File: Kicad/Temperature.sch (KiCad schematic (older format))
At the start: 2 parts

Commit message: Ready for Rev3 First layout review
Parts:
- removed TP11: CONN_1, symbol CONN_1
- R15: value 10K -> 1K
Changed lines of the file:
@@
 Sheet 4 7
 Title ""
-Date "11 oct 2014"
+Date "18 oct 2014"
 Rev ""
 Comp ""
@@
 P 3700 3300
 F 0 "R15" V 3780 3300 40  0000 C CNN
-F 1 "10K" V 3707 3301 40  0000 C CNN
+F 1 "1K" V 3707 3301 40  0000 C CNN
 F 2 "~" V 3630 3300 30  0000 C CNN
 F 3 "~" H 3700 3300 30  0000 C CNN
@@
 Text HLabel 1000 2700 0    60   Output ~ 0
 Therm+
-$Comp
-L CONN_1 TP11
-U 1 1 540E05A9
-P 3650 2300
-F 0 "TP11" H 3730 2300 40  0000 L CNN
-F 1 "CONN_1" H 3650 2355 30  0001 C CNN
-F 2 "" H 3650 2300 60  0000 C CNN
-F 3 "" H 3650 2300 60  0000 C CNN
-	1    3650 2300
-	1    0    0    -1
-$EndComp
 Wire Wire Line
 	950  3300 3450 3300
@@
 	4550 2700 4550 3300
 Connection ~ 4550 3300
-Wire Wire Line
-	3500 2300 3500 2700
-Connection ~ 3500 2700
 Wire Notes Line
 	6000 3100 6000 3500

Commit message: updated based on feedback. Ready for second review
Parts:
- added C3: .1, ~, symbol C
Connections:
- net AGND: now also C3.2
- new net V+_WallWart: C3.1
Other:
- note added: "Thermistor hangs off two of the 8 TB connectors."
- note removed: "To V+ WallWart"
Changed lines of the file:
@@
 Sheet 4 7
 Title ""
-Date "18 oct 2014"
+Date "21 oct 2014"
 Rev ""
 Comp ""
@@
 Therm-
 Connection ~ 2650 3300
-Text Notes 6200 3250 0    60   ~ 0
-To V+ WallWart
+Text HLabel 1250 1500 0    60   Input ~ 0
+V+_WallWart
+Text HLabel 8450 1500 2    60   Output ~ 0
+V+_WallWart_Out
+Wire Wire Line
+	1250 1500 8450 1500
+$Comp
+L C C3
+U 1 1 544542CF
+P 1750 1950
+F 0 "C3" H 1750 2050 40  0000 L CNN
+F 1 ".1" H 1756 1865 40  0000 L CNN
+F 2 "~" H 1788 1800 30  0000 C CNN
+F 3 "~" H 1750 1950 60  0000 C CNN
+	1    1750 1950
+	1    0    0    -1
+$EndComp
+Wire Wire Line
+	1750 1750 1750 1500
+Connection ~ 1750 1500
+$Comp
+L AGND #PWR05
+U 1 1 544542EA
+P 1750 2350
+F 0 "#PWR05" H 1750 2350 40  0001 C CNN
+F 1 "AGND" H 1750 2280 50  0000 C CNN
+F 2 "" H 1750 2350 60  0000 C CNN
+F 3 "" H 1750 2350 60  0000 C CNN
+	1    1750 2350
+	1    0    0    -1
+$EndComp
+Wire Wire Line
+	1750 2150 1750 2350
+Wire Notes Line
+	6000 3300 6500 3300
+Wire Notes Line
+	6500 3300 6500 1500
+Text Notes 6700 3000 0    60   ~ 0
+Thermistor hangs off two of the 8 TB connectors.
 $EndSCHEMATC

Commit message: before changing ADC
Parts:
- R15: value 1K -> 1K .1%
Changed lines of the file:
@@
 $Descr A4 11693 8268
 encoding utf-8
-Sheet 4 7
+Sheet 3 7
 Title ""
-Date "21 oct 2014"
+Date "10 nov 2014"
 Rev ""
 Comp ""
@@
 P 3700 3300
 F 0 "R15" V 3780 3300 40  0000 C CNN
-F 1 "1K" V 3707 3301 40  0000 C CNN
+F 1 "1K  .1%" V 3707 3301 40  0000 C CNN
 F 2 "~" V 3630 3300 30  0000 C CNN
 F 3 "~" H 3700 3300 30  0000 C CNN

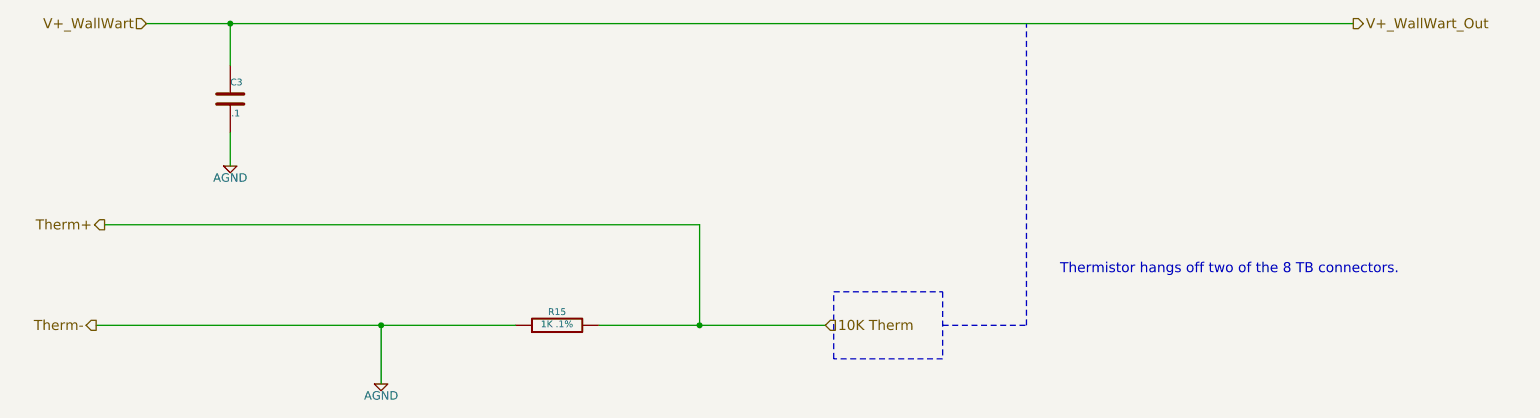
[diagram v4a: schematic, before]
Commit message: first pass changing ADC
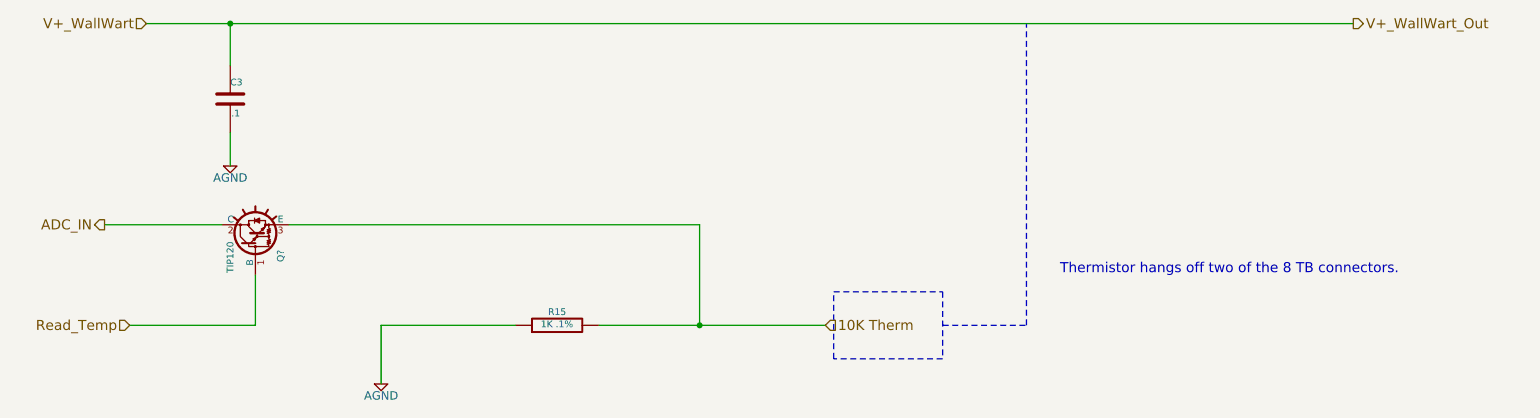
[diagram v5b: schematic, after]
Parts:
- added Q?: TIP120, TO220, symbol TIP120
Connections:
- net 10K Therm: now also Q?.3 (E)
- new net ADC_IN: Q?.2 (C)
- new net Read_Temp: Q?.1 (B)
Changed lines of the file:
@@
 Sheet 3 7
 Title ""
-Date "10 nov 2014"
+Date "11 nov 2014"
 Rev ""
 Comp ""
@@
 10K Therm
 Text HLabel 1000 2700 0    60   Output ~ 0
-Therm+
-Wire Wire Line
-	950  3300 3450 3300
+ADC_IN
 Wire Wire Line
 	2650 3300 2650 3650
 Wire Wire Line
 	3950 3300 5300 3300
-Wire Wire Line
-	1000 2700 4550 2700
 Wire Wire Line
 	4550 2700 4550 3300
@@
 Wire Notes Line
 	5350 3100 6000 3100
-Text HLabel 950  3300 0    60   Output ~ 0
-Therm-
-Connection ~ 2650 3300
 Text HLabel 1250 1500 0    60   Input ~ 0
 V+_WallWart
@@
 Text Notes 6700 3000 0    60   ~ 0
 Thermistor hangs off two of the 8 TB connectors.
+Wire Wire Line
+	3450 3300 2650 3300
+$Comp
+L TIP120 Q?
+U 1 1 5462158B
+P 1900 2800
+F 0 "Q?" H 1850 2650 40  0000 R CNN
+F 1 "TIP120" H 1900 2950 40  0000 R CNN
+F 2 "TO220" H 1780 2905 29  0001 C CNN
+F 3 "~" H 1900 2800 60  0000 C CNN
+	1    1900 2800
+	0    -1   -1   0
+$EndComp
+Wire Wire Line
+	2100 2700 4550 2700
+Wire Wire Line
+	1700 2700 1000 2700
+Text HLabel 1150 3300 0    60   Input ~ 0
+Read_Temp
+Wire Wire Line
+	1150 3300 1900 3300
+Wire Wire Line
+	1900 3300 1900 3000
 $EndSCHEMATC

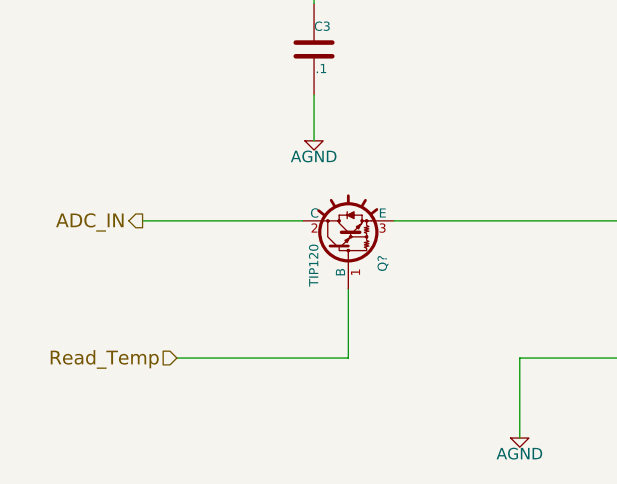
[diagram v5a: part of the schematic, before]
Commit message: prior to using Arduino ADC
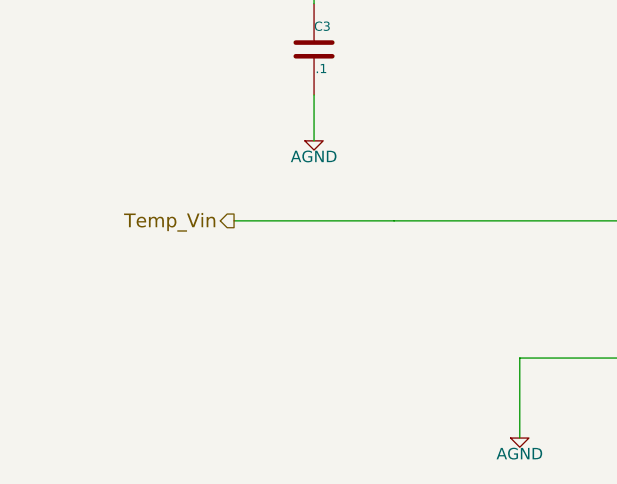
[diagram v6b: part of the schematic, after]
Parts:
- removed Q?: TIP120, TO220, symbol TIP120
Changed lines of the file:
@@
 Sheet 3 7
 Title ""
-Date "11 nov 2014"
+Date "12 nov 2014"
 Rev ""
 Comp ""
@@
 Text HLabel 5300 3300 2    60   Input ~ 0
 10K Therm
-Text HLabel 1000 2700 0    60   Output ~ 0
-ADC_IN
+Text HLabel 1400 2700 0    60   Output ~ 0
+Temp_Vin
 Wire Wire Line
 	2650 3300 2650 3650
@@
 Wire Wire Line
 	3450 3300 2650 3300
-$Comp
-L TIP120 Q?
-U 1 1 5462158B
-P 1900 2800
-F 0 "Q?" H 1850 2650 40  0000 R CNN
-F 1 "TIP120" H 1900 2950 40  0000 R CNN
-F 2 "TO220" H 1780 2905 29  0001 C CNN
-F 3 "~" H 1900 2800 60  0000 C CNN
-	1    1900 2800
-	0    -1   -1   0
-$EndComp
 Wire Wire Line
 	2100 2700 4550 2700
 Wire Wire Line
-	1700 2700 1000 2700
-Text HLabel 1150 3300 0    60   Input ~ 0
-Read_Temp
-Wire Wire Line
-	1150 3300 1900 3300
-Wire Wire Line
-	1900 3300 1900 3000
+	2100 2700 1400 2700
 $EndSCHEMATC
